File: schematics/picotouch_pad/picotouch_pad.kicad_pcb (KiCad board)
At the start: 2 copper layers, 207.5 x 38 mm, 100 parts, among them J1 AudioJack4, SW1 SSSS811101, U1 Pico, U2 MCP73831-2-OT, X1 AFC20-S02ACA-00

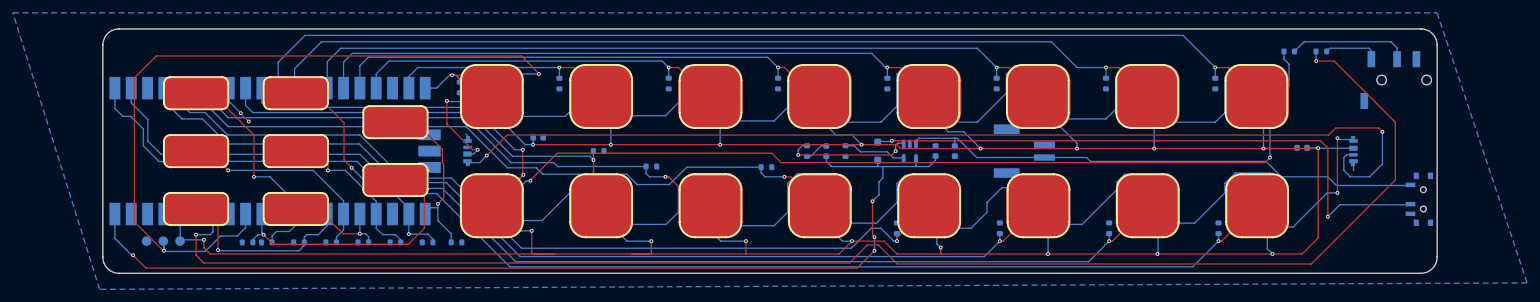
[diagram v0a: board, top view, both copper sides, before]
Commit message: add vbus diode, fix up power layout a bit
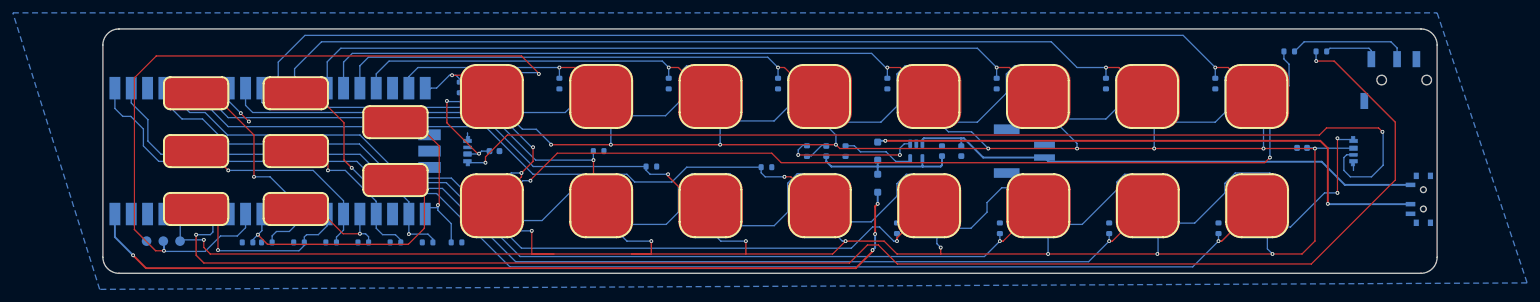
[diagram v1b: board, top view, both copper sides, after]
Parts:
- added D3: MBR120, Diode_SMD:D_SOD-123F, B.Cu at (134.6, 50.4)
- moved C18 7.12 mm to (75.0, 45.4)
- moved C19 1.00 mm to (147.6, 45.4)
- moved C20 1.00 mm to (144.6, 45.4)
- moved U2 1.00 mm to (140.6, 45.4)
- moved LED1 0.40 mm to (78.6, 36.0)
- moved LED9 0.40 mm to (78.6, 52.9)
- moved LED11 0.08 mm to (112.6, 52.9)
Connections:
- U1 pad 40: +5V -> VBUS
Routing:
- net +5V: track 161.3 -> 24.1 mm, vias 4 -> 0
- net VBUS: track 0.00 -> 134.9 mm, vias 0 -> 4
- net +3.3V: track 612.9 -> 609.6 mm
- net Net-(D2-A): track 94.5 -> 92.1 mm
- net /TOUCH9: track 58.7 -> 60.9 mm
- net Net-(U2-PROG): track 9.61 -> 11.5 mm
- net Net-(LED1-DOUT): track 30.8 -> 29.5 mm
- net Net-(U2-STAT): track 20.0 -> 21.2 mm
- net Net-(LED17-DOUT): track 160.7 -> 161.5 mm
- net Net-(LED12-DOUT): track 28.0 -> 27.4 mm
- net /TOUCH18: track 37.1 -> 37.7 mm
- net /TOUCH17: track 26.9 -> 26.3 mm
- net +BATT: track 81.4 -> 80.9 mm
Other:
- board text added: "ON/OFF"

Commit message: cleanup and new silkscreen
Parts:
- added C18: 100n, Capacitor_SMD:C_0603_1608Metric, B.Cu at (208.6, 61.4)
- added G***: LOGO, LOGO, F.Cu at (117.8, 45.4)
- added H1: MountingHole, MountingHole:MountingHole_2.7mm_M2.5, F.Cu at (17.1, 29.4)
- added H2: MountingHole, MountingHole:MountingHole_2.7mm_M2.5, F.Cu at (218.6, 61.4)
- added LED18: SK6812SIDE, todbot_stuff:LED-SMD_4P-L4.0-W1.6-L-keepoutrev, B.Cu at (208.7, 56.6)
- moved SW1 0.10 mm to (219.0, 52.8)
- renumbered C18 to C19, C19 to C20, C20 to C21, LED18 to LED19
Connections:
- LED19 pad 1: Net-(LED17-DOUT) -> Net-(LED18-DIN)
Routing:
- net Net-(LED18-DIN): track 0.00 -> 166.3 mm, vias 0 -> 4
- net Net-(LED17-DOUT): track 161.5 -> 12.0 mm
- net +3.3V: track 609.6 -> 617.6 mm, vias 20 -> 21
- net /MIDI_OUT: track 231.2 -> 235.3 mm
- net GND: track 25.6 -> 27.9 mm

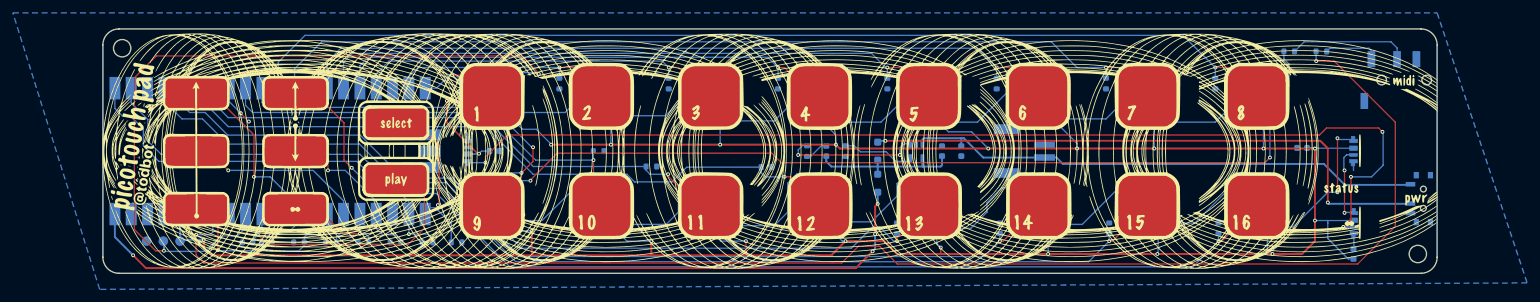
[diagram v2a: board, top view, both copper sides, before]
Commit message: more layout tuning
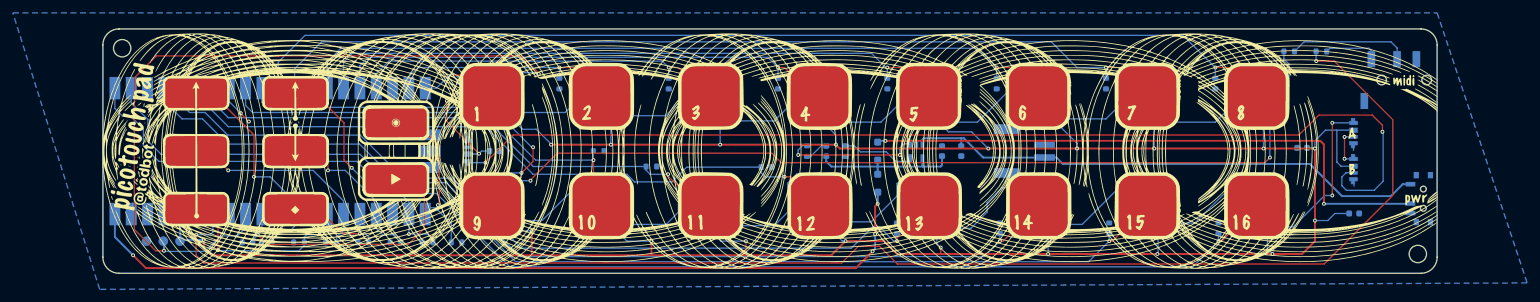
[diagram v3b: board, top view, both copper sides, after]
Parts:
- moved LED18 8.40 mm to (208.6, 48.2)
- moved C18 6.30 mm to (208.7, 55.1), turned to 0 degrees
- moved LED17 2.80 mm to (208.6, 42.6)
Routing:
- net Net-(LED17-DOUT): track 12.0 -> 6.74 mm
- net /MIDI_OUT: track 235.3 -> 231.9 mm
- net Net-(LED16-DOUT): track 27.8 -> 30.4 mm
- net GND: track 27.9 -> 26.1 mm
- net +BATT: track 80.9 -> 82.3 mm
- net +3.3V: track 617.6 -> 618.9 mm
- net Net-(LED18-DIN): track 166.3 -> 165.6 mm, vias 4 -> 2

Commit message: one net forgot! fix +5V to VSYS
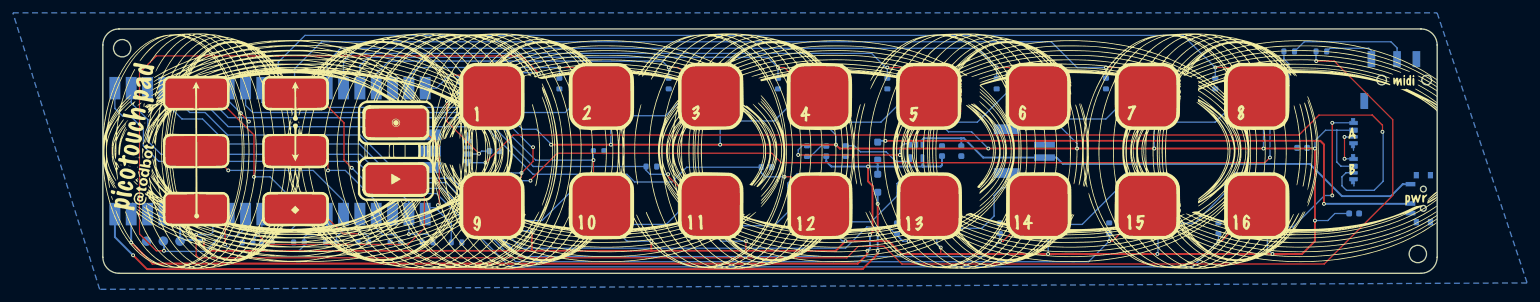
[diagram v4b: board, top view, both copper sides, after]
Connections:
- U1 pad 39: unconnected-(U1-VSYS-Pad39) -> +5V
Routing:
- net +5V: track 24.1 -> 160.2 mm, vias 0 -> 4
- net +3.3V: track 618.9 -> 616.8 mm
- net /TOUCH13: track 133.3 -> 134.7 mm
- net /TOUCH22: track 31.4 -> 30.2 mm
- net Net-(LED13-DOUT): track 27.6 -> 28.6 mm
- net VBUS: track 134.9 -> 135.7 mm
- net /LED_DAT: track 119.6 -> 118.8 mm
- net /MIDI_OUT: track 231.9 -> 231.2 mm
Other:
- board text added: "picotouch_pad - USB MIDI controller / macropad 14 Dec 2024 - @todbot / Tod Kurt github.com/todbot/picotouch_pad Uses Pico RP2040"
- board text removed: "picotouch_pad - USB MIDI controller / macropad 22 Sep 2024 - @todbot / Tod Kurt github.com/todbot/picotouch_pad Uses Pico RP2040"
